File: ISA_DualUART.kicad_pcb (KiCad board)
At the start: 2 copper layers, 176.5 x 90.2 mm, 74 parts, among them J1 ISA BUS, J10 Parallel Port, J2 ADDR_IRQ, J3 UART1_SEL, J4 UART2_SEL, J6 Serial 2 IDC, J7 Serial 1 DB9, J9 Parport IRQ Select, U1 74LS138, U11 74LS30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

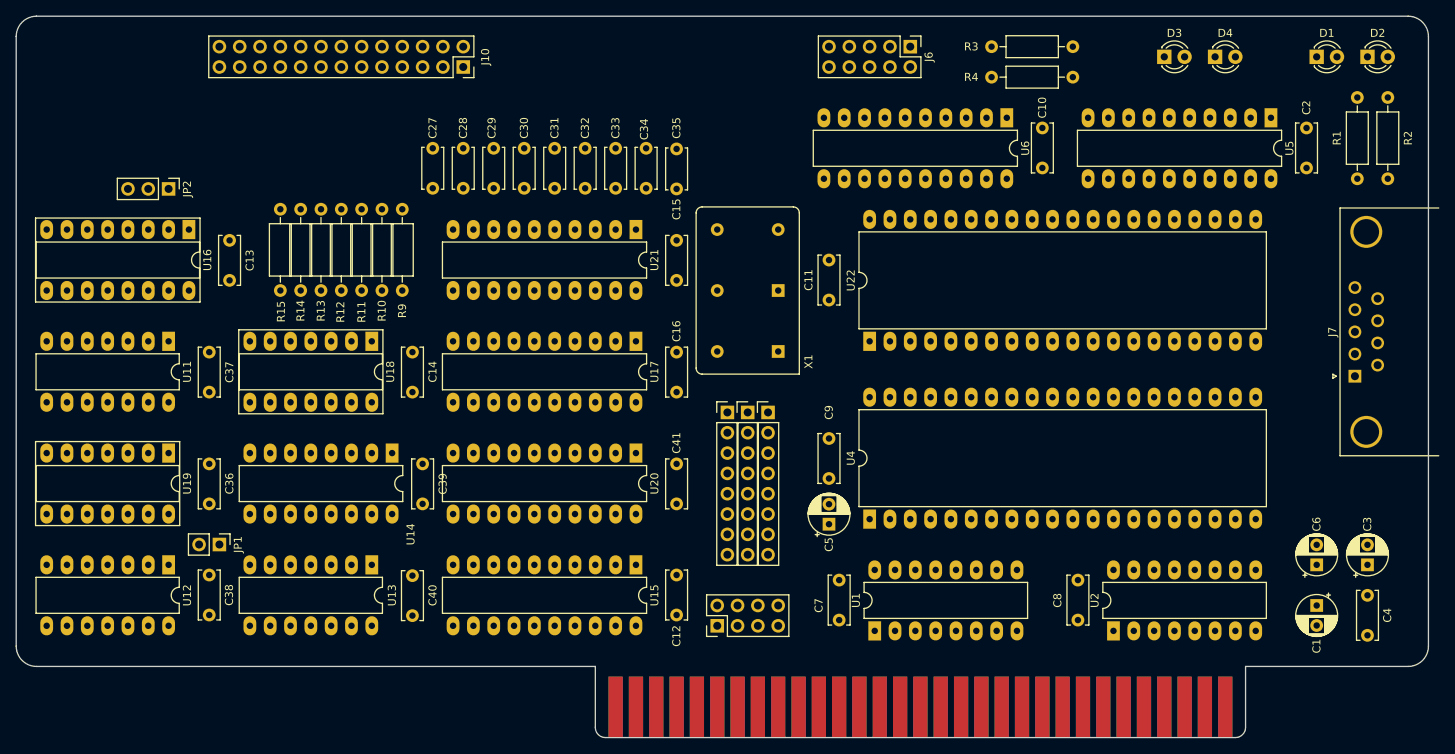
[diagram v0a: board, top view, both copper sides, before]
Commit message: Moved around some components
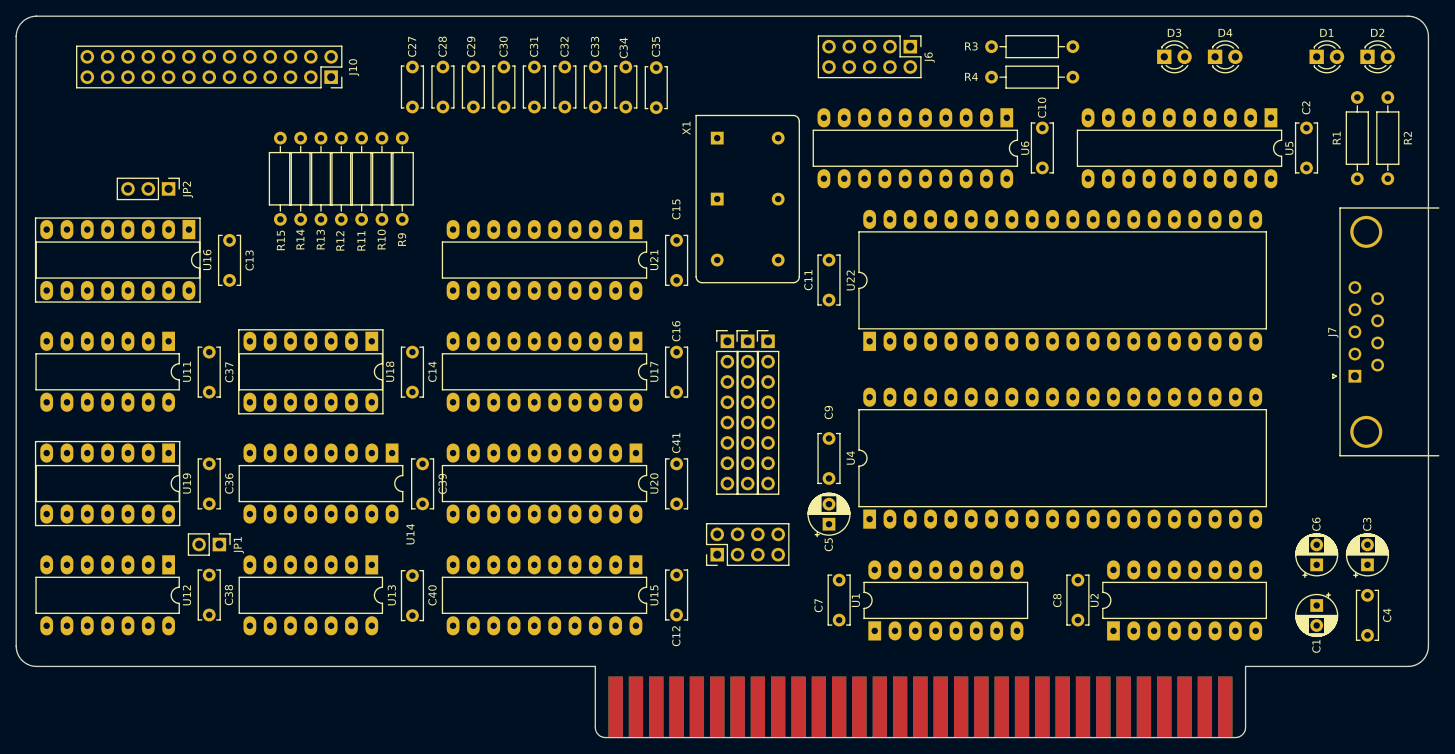
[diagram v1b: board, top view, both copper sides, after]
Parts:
- moved X1 27.7 mm to (226.1, 128.3), turned to 270 degrees
- moved J10 16.6 mm to (177.8, 120.7)
- moved C35 10.5 mm to (218.4, 124.5)
- moved C30 10.5 mm to (199.4, 119.4)
- moved C31 10.5 mm to (203.2, 119.4)
- moved C32 10.5 mm to (207.0, 119.4)
- moved C33 10.5 mm to (210.8, 119.4)
- moved C27 10.5 mm to (188.0, 119.4)
- moved C28 10.5 mm to (191.8, 119.4)
- moved C29 10.5 mm to (195.6, 119.4)
- moved C34 10.5 mm to (214.6, 119.4)
- moved J2 8.89 mm to (229.9, 153.7)
- moved J3 8.89 mm to (227.3, 153.7)
- moved J4 8.89 mm to (232.4, 153.7)
- moved J9 8.89 mm to (226.1, 180.3)
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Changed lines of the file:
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@@
   )
   (module Connector_PinHeader_2.54mm:PinHeader_2x04_P2.54mm_Vertical (layer F.Cu)
-    (at 226.06 189.23 90)
+    (at 226.06 180.34 90)
     (descr "Through hole straight pin header, 2x04, 2.54mm pitch, double rows")
     (tags "Through hole pin header THT 2x04 2.54mm double row")
@@
   )
   (module Resistor_THT:R_Axial_DIN0207_L6.3mm_D2.5mm_P10.16mm_Horizontal (layer F.Cu)
-    (at 171.45 137.16 270)
+    (at 171.45 128.27 270)
     (descr "Resistor, Axial_DIN0207 series, Axial, Horizontal, pin pitch=10.16mm, 0.25W = 1/4W, length*diameter=6.3*2.5mm^2, http://cdn-reichelt.de/documents/datenblatt/B400/1_4W%23YAG.pdf")
     (tags "Resistor Axial_DIN0207 series Axial Horizontal pin pitch 10.16mm 0.25W = 1/4W length 6.3mm diameter 2.5mm")
@@
   )
   (module Resistor_THT:R_Axial_DIN0207_L6.3mm_D2.5mm_P10.16mm_Horizontal (layer F.Cu)
-    (at 173.99 137.16 270)
+    (at 173.99 128.27 270)
     (descr "Resistor, Axial_DIN0207 series, Axial, Horizontal, pin pitch=10.16mm, 0.25W = 1/4W, length*diameter=6.3*2.5mm^2, http://cdn-reichelt.de/documents/datenblatt/B400/1_4W%23YAG.pdf")
     (tags "Resistor Axial_DIN0207 series Axial Horizontal pin pitch 10.16mm 0.25W = 1/4W length 6.3mm diameter 2.5mm")
@@
   )
   (module Resistor_THT:R_Axial_DIN0207_L6.3mm_D2.5mm_P10.16mm_Horizontal (layer F.Cu)
-    (at 176.53 137.16 270)
+    (at 176.53 128.27 270)
     (descr "Resistor, Axial_DIN0207 series, Axial, Horizontal, pin pitch=10.16mm, 0.25W = 1/4W, length*diameter=6.3*2.5mm^2, http://cdn-reichelt.de/documents/datenblatt/B400/1_4W%23YAG.pdf")
     (tags "Resistor Axial_DIN0207 series Axial Horizontal pin pitch 10.16mm 0.25W = 1/4W length 6.3mm diameter 2.5mm")
@@
   )
   (module Resistor_THT:R_Axial_DIN0207_L6.3mm_D2.5mm_P10.16mm_Horizontal (layer F.Cu)
-    (at 179.07 137.16 270)
+    (at 179.07 128.27 270)
     (descr "Resistor, Axial_DIN0207 series, Axial, Horizontal, pin pitch=10.16mm, 0.25W = 1/4W, length*diameter=6.3*2.5mm^2, http://cdn-reichelt.de/documents/datenblatt/B400/1_4W%23YAG.pdf")
     (tags "Resistor Axial_DIN0207 series Axial Horizontal pin pitch 10.16mm 0.25W = 1/4W length 6.3mm diameter 2.5mm")
@@
   )
   (module Resistor_THT:R_Axial_DIN0207_L6.3mm_D2.5mm_P10.16mm_Horizontal (layer F.Cu)
-    (at 181.61 137.16 270)
+    (at 181.61 128.27 270)
     (descr "Resistor, Axial_DIN0207 series, Axial, Horizontal, pin pitch=10.16mm, 0.25W = 1/4W, length*diameter=6.3*2.5mm^2, http://cdn-reichelt.de/documents/datenblatt/B400/1_4W%23YAG.pdf")
     (tags "Resistor Axial_DIN0207 series Axial Horizontal pin pitch 10.16mm 0.25W = 1/4W length 6.3mm diameter 2.5mm")
@@
   )
   (module Resistor_THT:R_Axial_DIN0207_L6.3mm_D2.5mm_P10.16mm_Horizontal (layer F.Cu)
-    (at 184.15 137.16 270)
+    (at 184.15 128.27 270)
     (descr "Resistor, Axial_DIN0207 series, Axial, Horizontal, pin pitch=10.16mm, 0.25W = 1/4W, length*diameter=6.3*2.5mm^2, http://cdn-reichelt.de/documents/datenblatt/B400/1_4W%23YAG.pdf")
     (tags "Resistor Axial_DIN0207 series Axial Horizontal pin pitch 10.16mm 0.25W = 1/4W length 6.3mm diameter 2.5mm")
@@
   )
   (module Resistor_THT:R_Axial_DIN0207_L6.3mm_D2.5mm_P10.16mm_Horizontal (layer F.Cu)
-    (at 186.69 137.16 270)
+    (at 186.69 128.27 270)
     (descr "Resistor, Axial_DIN0207 series, Axial, Horizontal, pin pitch=10.16mm, 0.25W = 1/4W, length*diameter=6.3*2.5mm^2, http://cdn-reichelt.de/documents/datenblatt/B400/1_4W%23YAG.pdf")
     (tags "Resistor Axial_DIN0207 series Axial Horizontal pin pitch 10.16mm 0.25W = 1/4W length 6.3mm diameter 2.5mm")
@@
   )
   (module Connector_PinSocket_2.54mm:PinSocket_2x13_P2.54mm_Vertical (layer F.Cu)
-    (at 194.31 119.38 270)
+    (at 177.8 120.65 270)
     (descr "Through hole straight socket strip, 2x13, 2.54mm pitch, double cols (from Kicad 4.0.7), script generated")
     (tags "Through hole socket strip THT 2x13 2.54mm double row")
@@
   )
   (module Capacitor_THT:C_Disc_D5.0mm_W2.5mm_P5.00mm (layer F.Cu)
-    (at 220.98 134.62 90)
+    (at 218.44 124.46 90)
     (descr "C, Disc series, Radial, pin pitch=5.00mm, , diameter*width=5*2.5mm^2, Capacitor, http://cdn-reichelt.de/documents/datenblatt/B300/DS_KERKO_TC.pdf")
     (tags "C Disc series Radial pin pitch 5.00mm  diameter 5mm width 2.5mm Capacitor")
@@
   )
   (module Capacitor_THT:C_Disc_D5.0mm_W2.5mm_P5.00mm (layer F.Cu)
-    (at 217.17 129.54 270)
+    (at 214.63 119.38 270)
     (descr "C, Disc series, Radial, pin pitch=5.00mm, , diameter*width=5*2.5mm^2, Capacitor, http://cdn-reichelt.de/documents/datenblatt/B300/DS_KERKO_TC.pdf")
     (tags "C Disc series Radial pin pitch 5.00mm  diameter 5mm width 2.5mm Capacitor")
@@
   )
   (module Capacitor_THT:C_Disc_D5.0mm_W2.5mm_P5.00mm (layer F.Cu)
-    (at 213.36 129.54 270)
+    (at 210.82 119.38 270)
     (descr "C, Disc series, Radial, pin pitch=5.00mm, , diameter*width=5*2.5mm^2, Capacitor, http://cdn-reichelt.de/documents/datenblatt/B300/DS_KERKO_TC.pdf")
     (tags "C Disc series Radial pin pitch 5.00mm  diameter 5mm width 2.5mm Capacitor")
@@
   )
   (module Capacitor_THT:C_Disc_D5.0mm_W2.5mm_P5.00mm (layer F.Cu)
-    (at 209.55 129.54 270)
+    (at 207.01 119.38 270)
     (descr "C, Disc series, Radial, pin pitch=5.00mm, , diameter*width=5*2.5mm^2, Capacitor, http://cdn-reichelt.de/documents/datenblatt/B300/DS_KERKO_TC.pdf")
     (tags "C Disc series Radial pin pitch 5.00mm  diameter 5mm width 2.5mm Capacitor")
@@
   )
   (module Capacitor_THT:C_Disc_D5.0mm_W2.5mm_P5.00mm (layer F.Cu)
-    (at 205.74 129.54 270)
+    (at 203.2 119.38 270)
     (descr "C, Disc series, Radial, pin pitch=5.00mm, , diameter*width=5*2.5mm^2, Capacitor, http://cdn-reichelt.de/documents/datenblatt/B300/DS_KERKO_TC.pdf")
     (tags "C Disc series Radial pin pitch 5.00mm  diameter 5mm width 2.5mm Capacitor")
@@
   )
   (module Capacitor_THT:C_Disc_D5.0mm_W2.5mm_P5.00mm (layer F.Cu)
-    (at 201.93 129.54 270)
+    (at 199.39 119.38 270)
     (descr "C, Disc series, Radial, pin pitch=5.00mm, , diameter*width=5*2.5mm^2, Capacitor, http://cdn-reichelt.de/documents/datenblatt/B300/DS_KERKO_TC.pdf")
     (tags "C Disc series Radial pin pitch 5.00mm  diameter 5mm width 2.5mm Capacitor")
@@
   )
   (module Capacitor_THT:C_Disc_D5.0mm_W2.5mm_P5.00mm (layer F.Cu)
-    (at 198.12 129.54 270)
+    (at 195.58 119.38 270)
     (descr "C, Disc series, Radial, pin pitch=5.00mm, , diameter*width=5*2.5mm^2, Capacitor, http://cdn-reichelt.de/documents/datenblatt/B300/DS_KERKO_TC.pdf")
     (tags "C Disc series Radial pin pitch 5.00mm  diameter 5mm width 2.5mm Capacitor")
@@
   )
   (module Capacitor_THT:C_Disc_D5.0mm_W2.5mm_P5.00mm (layer F.Cu)
-    (at 194.31 129.54 270)
+    (at 191.77 119.38 270)
     (descr "C, Disc series, Radial, pin pitch=5.00mm, , diameter*width=5*2.5mm^2, Capacitor, http://cdn-reichelt.de/documents/datenblatt/B300/DS_KERKO_TC.pdf")
     (tags "C Disc series Radial pin pitch 5.00mm  diameter 5mm width 2.5mm Capacitor")
@@
   )
   (module Capacitor_THT:C_Disc_D5.0mm_W2.5mm_P5.00mm (layer F.Cu)
-    (at 190.5 129.54 270)
+    (at 187.96 119.38 270)
     (descr "C, Disc series, Radial, pin pitch=5.00mm, , diameter*width=5*2.5mm^2, Capacitor, http://cdn-reichelt.de/documents/datenblatt/B300/DS_KERKO_TC.pdf")
     (tags "C Disc series Radial pin pitch 5.00mm  diameter 5mm width 2.5mm Capacitor")
@@
   )
   (module ISA_DualUART:Oscillator_DIP-14-8 (layer F.Cu)
-    (at 233.68 154.94 90)
+    (at 226.06 128.27 270)
     (descr "Oscillator, DIP14, http://cdn-reichelt.de/documents/datenblatt/B400/OSZI.pdf")
     (tags oscillator)
@@
       (effects (font (size 1 1) (thickness 0.15)))
     )
-    (pad 1 thru_hole rect (at 7.62 0 90) (size 1.6 1.6) (drill 0.8) (layers *.Cu *.Mask)
+    (pad 1 thru_hole rect (at 7.62 0 270) (size 1.6 1.6) (drill 0.8) (layers *.Cu *.Mask)
       (net 77 "Net-(X1-Pad1)"))
-    (pad 14 thru_hole circle (at 7.62 -7.62 90) (size 1.6 1.6) (drill 0.8) (layers *.Cu *.Mask)
-      (net 4 VCC))
-    (pad 7 thru_hole circle (at 15.24 0 90) (size 1.6 1.6) (drill 0.8) (layers *.Cu *.Mask)
-      (net 2 GND))
-    (pad 8 thru_hole circle (at 15.24 -7.62 90) (size 1.6 1.6) (drill 0.8) (layers *.Cu *.Mask)
+    (pad 14 thru_hole circle (at 7.62 -7.62 270) (size 1.6 1.6) (drill 0.8) (layers *.Cu *.Mask)
+      (net 4 VCC))
+    (pad 7 thru_hole circle (at 15.24 0 270) (size 1.6 1.6) (drill 0.8) (layers *.Cu *.Mask)
+      (net 2 GND))
+    (pad 8 thru_hole circle (at 15.24 -7.62 270) (size 1.6 1.6) (drill 0.8) (layers *.Cu *.Mask)
       (net 67 /SER_CLK))
-    (pad 14 thru_hole circle (at 0 -7.62 90) (size 1.6 1.6) (drill 0.8) (layers *.Cu *.Mask)
-      (net 4 VCC))
-    (pad 1 thru_hole rect (at 0 0 90) (size 1.6 1.6) (drill 0.8) (layers *.Cu *.Mask)
+    (pad 14 thru_hole circle (at 0 -7.62 270) (size 1.6 1.6) (drill 0.8) (layers *.Cu *.Mask)
+      (net 4 VCC))
+    (pad 1 thru_hole rect (at 0 0 270) (size 1.6 1.6) (drill 0.8) (layers *.Cu *.Mask)
       (net 77 "Net-(X1-Pad1)"))
     (model ${KISYS3DMOD}/Oscillator.3dshapes/Oscillator_DIP-14.wrl
@@
   )
   (module Connector_PinHeader_2.54mm:PinHeader_1x08_P2.54mm_Vertical (layer F.Cu)
-    (at 232.41 162.56)
+    (at 232.41 153.67)
     (descr "Through hole straight pin header, 1x08, 2.54mm pitch, single row")
     (tags "Through hole pin header THT 1x08 2.54mm single row")
@@
   )
   (module Connector_PinHeader_2.54mm:PinHeader_1x08_P2.54mm_Vertical locked (layer F.Cu)
-    (at 227.33 162.56)
+    (at 227.33 153.67)
     (descr "Through hole straight pin header, 1x08, 2.54mm pitch, single row")
     (tags "Through hole pin header THT 1x08 2.54mm single row")
@@
   )
   (module Connector_PinHeader_2.54mm:PinHeader_1x08_P2.54mm_Vertical (layer F.Cu)
-    (at 229.87 162.56)
+    (at 229.87 153.67)
     (descr "Through hole straight pin header, 1x08, 2.54mm pitch, single row")
     (tags "Through hole pin header THT 1x08 2.54mm single row")
